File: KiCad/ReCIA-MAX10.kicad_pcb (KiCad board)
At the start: 4 copper layers, 17.4 x 51.4 mm, 15 parts, among them J1 Conn_02x03_Odd_Even, U1 AMS1117-3.3, U2 SN74CBT16210, U3 SN74CBT16210, U4 10M02SCU169, U5 8520_DIP_SOCKET

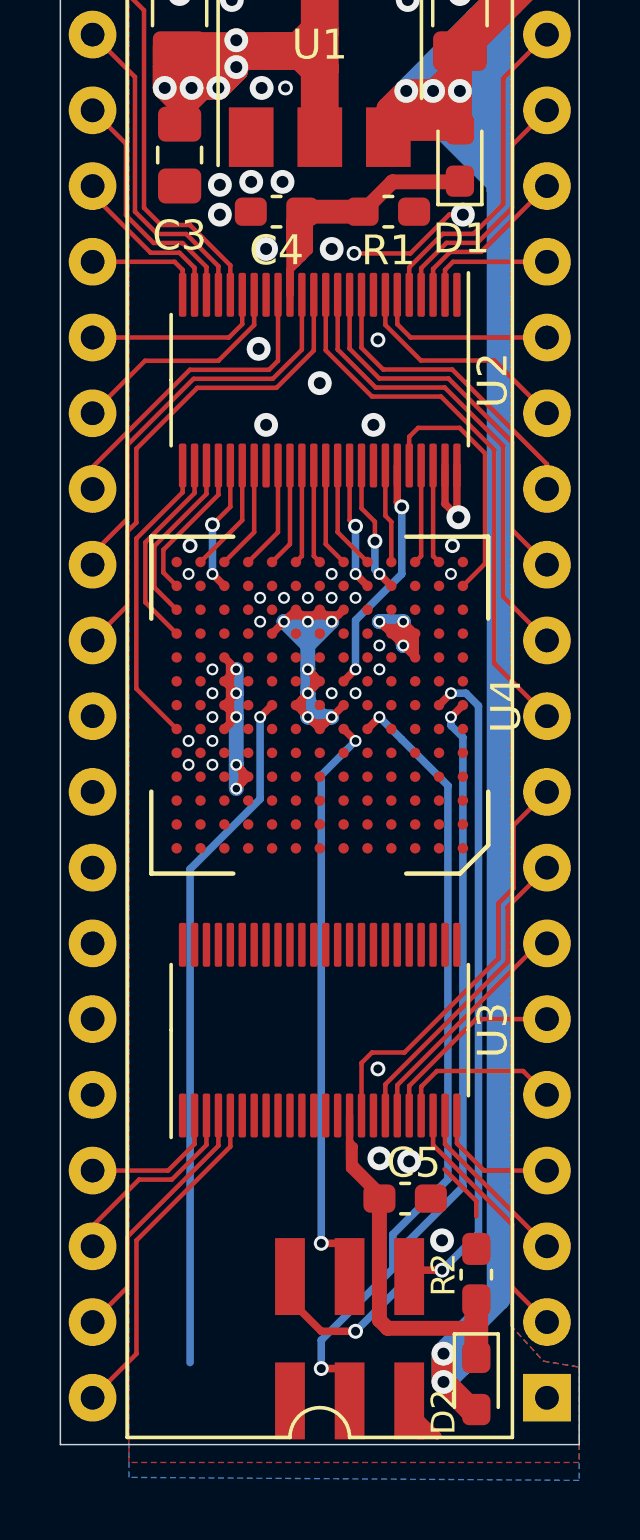
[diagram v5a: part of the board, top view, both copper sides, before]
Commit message: add XTAL to design
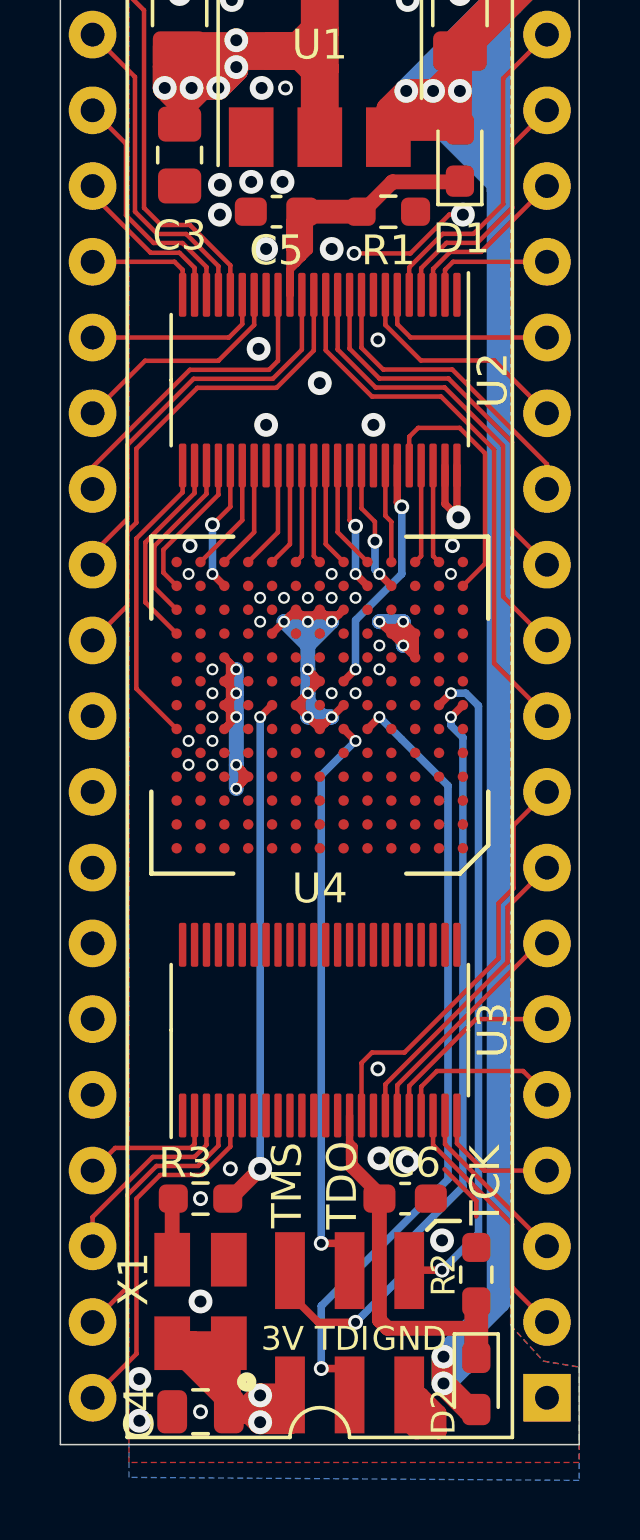
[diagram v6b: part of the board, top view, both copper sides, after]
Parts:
- added C4: 0.1uF, Capacitor_SMD:C_0805_2012Metric, F.Cu at (128.0, 107.6)
- added R3: 33, Resistor_SMD:R_0603_1608Metric_Pad0.98x0.95mm_HandSolder, F.Cu at (128.0, 100.5)
- added X1: Oscillator_3.2x2.5mm-28.6363MHz, Oscillator:Oscillator_SMD_SeikoEpson_SG8002CE-4Pin_3.2x2.5mm, F.Cu at (128.0, 103.9)
- R1, R2: footprint Capacitor_SMD:C_0603_1608Metric_Pad1.08x0.95mm_HandSolder -> Resistor_SMD:R_0603_1608Metric_Pad0.98x0.95mm_HandSolder
- moved J1 0.20 mm to (133.0, 105.0)
- renumbered C4 to C5, C5 to C6
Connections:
- U4 pad G9: OSC_CLK -> XTAL_28M
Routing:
- net OSC_CLK: track 23.2 -> 0.00 mm, vias 1 -> 0
- net 3V3: track 84.2 -> 102.0 mm, vias 20 -> 22
- net XTAL_28M: track 0.00 -> 17.2 mm, vias 0 -> 2
- net Net-(R3-Pad1): track 0.00 -> 2.07 mm
- net SP: track 8.68 -> 9.50 mm
- net CNT: track 11.4 -> 12.2 mm
- net GND: track 15.4 -> 15.8 mm, vias 48 -> 54
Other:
- board text added: "3V"
- board text added: "GND"
- board text added: "TCK"
- board text added: "TDI"
- board text added: "TDO"
- board text added: "TMS"

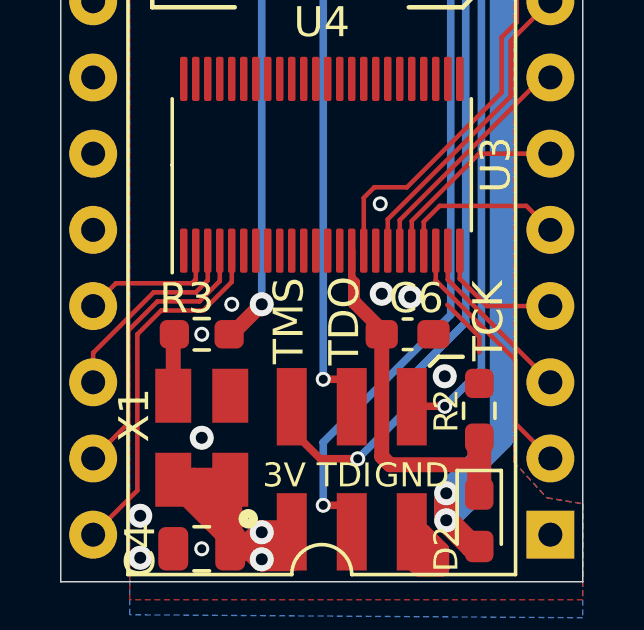
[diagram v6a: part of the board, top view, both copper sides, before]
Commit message: add XTAL step file to 3D Setting for X1
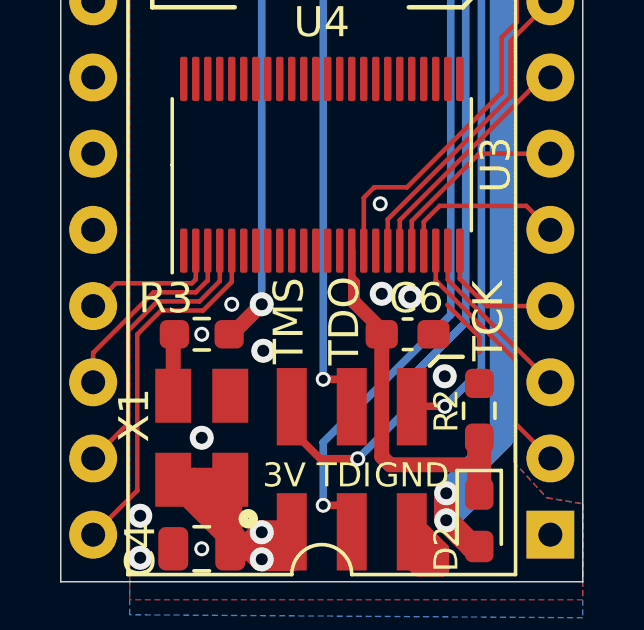
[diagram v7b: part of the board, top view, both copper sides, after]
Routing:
- net GND: vias 54 -> 55

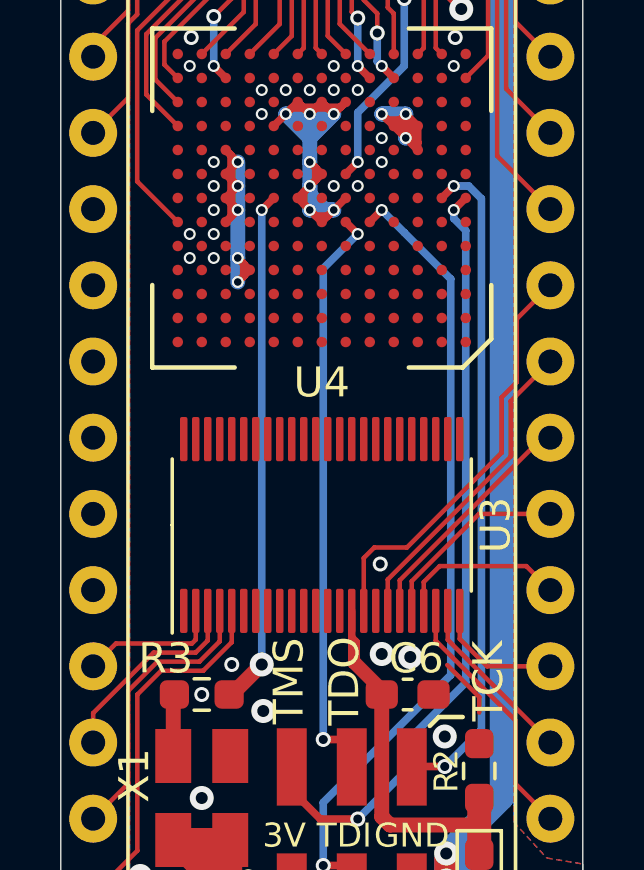
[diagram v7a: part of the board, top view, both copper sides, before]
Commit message: re-routed XTAL trace with 15 mil trace
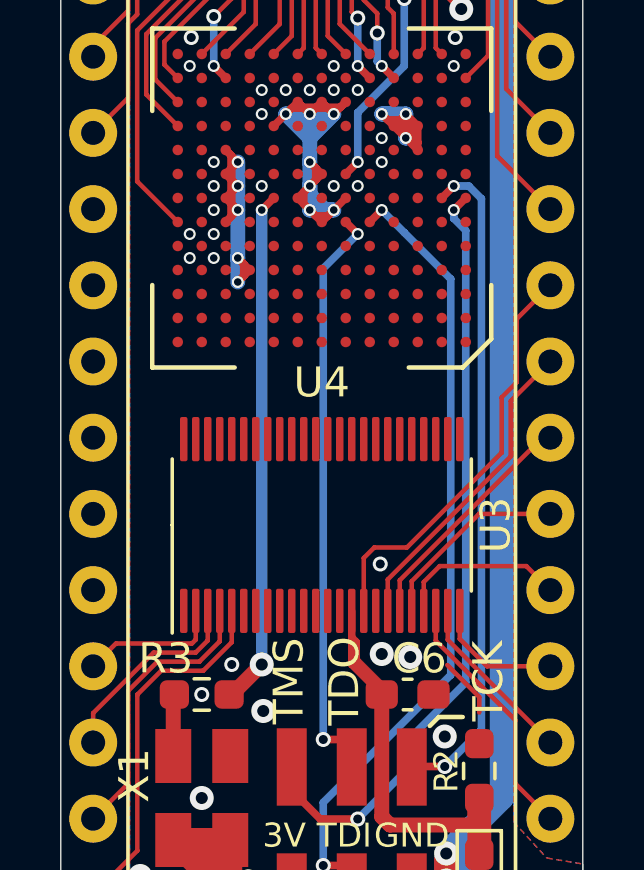
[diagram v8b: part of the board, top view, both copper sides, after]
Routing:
- net GND: vias 55 -> 56
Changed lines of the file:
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@@
     (thickness 1.6)
     (drawings 12)
-    (tracks 619)
+    (tracks 620)
     (zones 0)
     (modules 18)
@@
   )
   (setup
-    (last_trace_width 0.1524)
+    (last_trace_width 0.254)
     (user_trace_width 0.2)
     (user_trace_width 0.25)
     (user_trace_width 0.254)
+    (user_trace_width 0.381)
     (user_trace_width 0.5)
     (user_trace_width 0.8)
@@
     (tags "capacitor handsolder")
     (attr smd)
-    (fp_text reference C6 (at 0.2875 -1.2) (layer F.SilkS)
+    (fp_text reference C6 (at 0.3875 -1.2) (layer F.SilkS)
       (effects (font (size 1 1) (thickness 0.15)))
     )
@@
   (via (at 128 100.45) (size 0.5) (drill 0.3) (layers F.Cu B.Cu) (net 2))
   (via (at 130.05 101) (size 0.8) (drill 0.4) (layers F.Cu B.Cu) (net 2))
+  (via (at 130 83.5) (size 0.4) (drill 0.25) (layers F.Cu B.Cu) (net 2))
   (segment (start 128.2 98.65) (end 128.2 97.6625) (width 0.1524) (layer F.Cu) (net 3))
   (segment (start 124.38 102.05) (end 124.38 101.07) (width 0.1524) (layer F.Cu) (net 3))
@@
   (segment (start 127.05 102.5) (end 127.05 100.4875) (width 0.5) (layer F.Cu) (net 201))
   (via (at 130 84.3) (size 0.4) (drill 0.25) (layers F.Cu B.Cu) (net 202))
-  (segment (start 130 84.3) (end 130.4 83.9) (width 0.254) (layer F.Cu) (net 202))
   (via (at 130 99.45) (size 0.8) (drill 0.4) (layers F.Cu B.Cu) (net 202))
   (segment (start 129 100.45) (end 130 99.45) (width 0.5) (layer F.Cu) (net 202))
   (segment (start 128.9125 100.45) (end 129 100.45) (width 0.5) (layer F.Cu) (net 202))
-  (segment (start 130 84.3) (end 130 99.45) (width 0.254) (layer B.Cu) (net 202))
+  (segment (start 130 99.45) (end 130 84.3) (width 0.381) (layer B.Cu) (net 202))
+  (segment (start 130 84.3) (end 130.4 83.9) (width 0.254) (layer F.Cu) (net 202))
   (zone (net 2) (net_name GND) (layer F.Cu) (hatch edge 0.508)
     (connect_pads (clearance 0.15))
